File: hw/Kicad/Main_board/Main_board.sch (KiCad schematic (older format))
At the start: 27 parts, among them J1 LIPO 2S, J10 DIST_FRONT, J11 SENSORES_LINEA, J12 DIST_DCHA, J2 MOT_IZQ, J3 TB6612FNG_A, J4 TB6612FNG_B, J5 DC-DC_5V, J6 HC-05, J7 MOT_DER, J8 DIST_IZQ, J9 CAMARA, SW1 SW_DPDT, SW2 SW_Push, SW3 SW_Push, U1 PCF8574

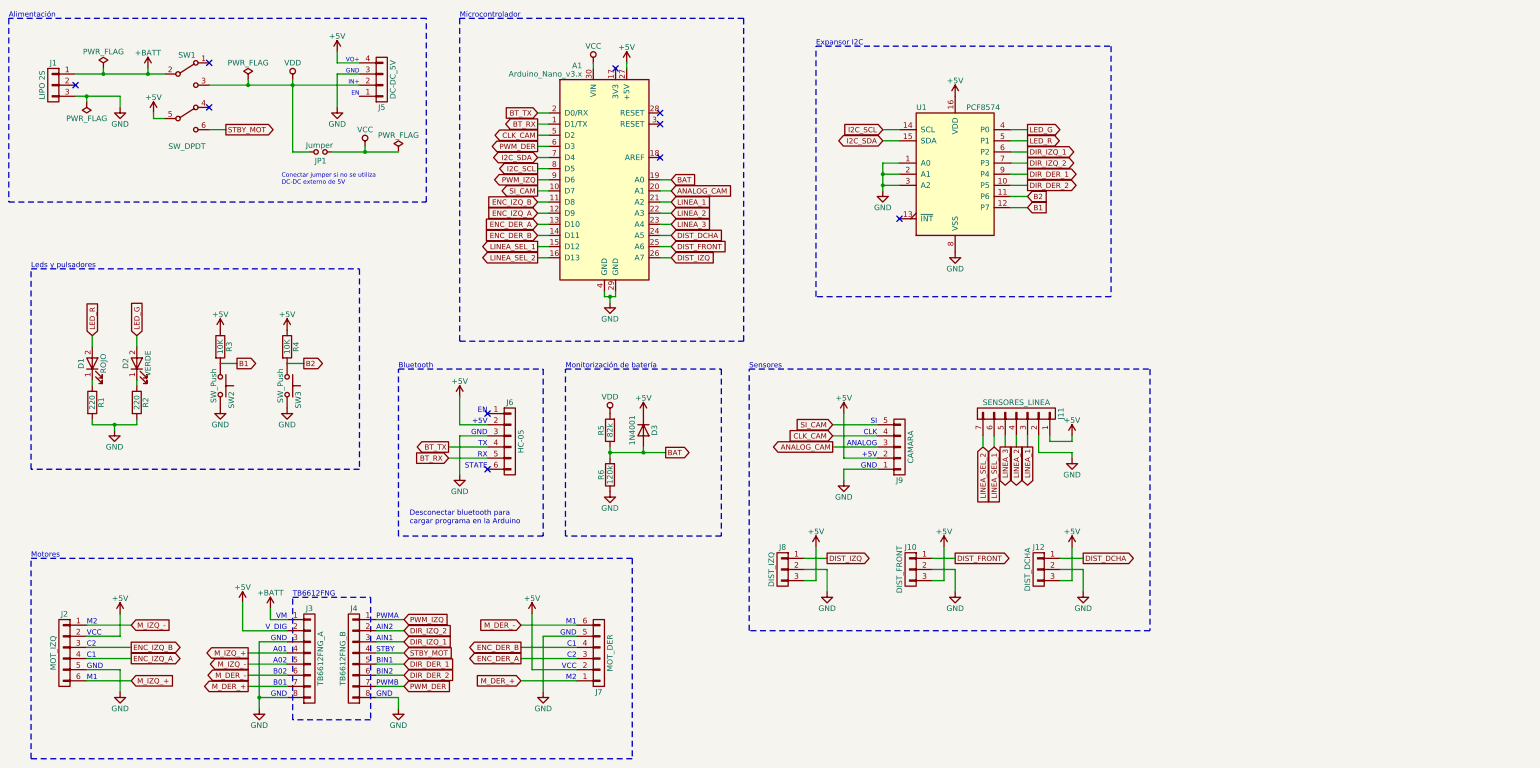
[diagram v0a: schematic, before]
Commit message: Leds connections modified and I2C resistors added
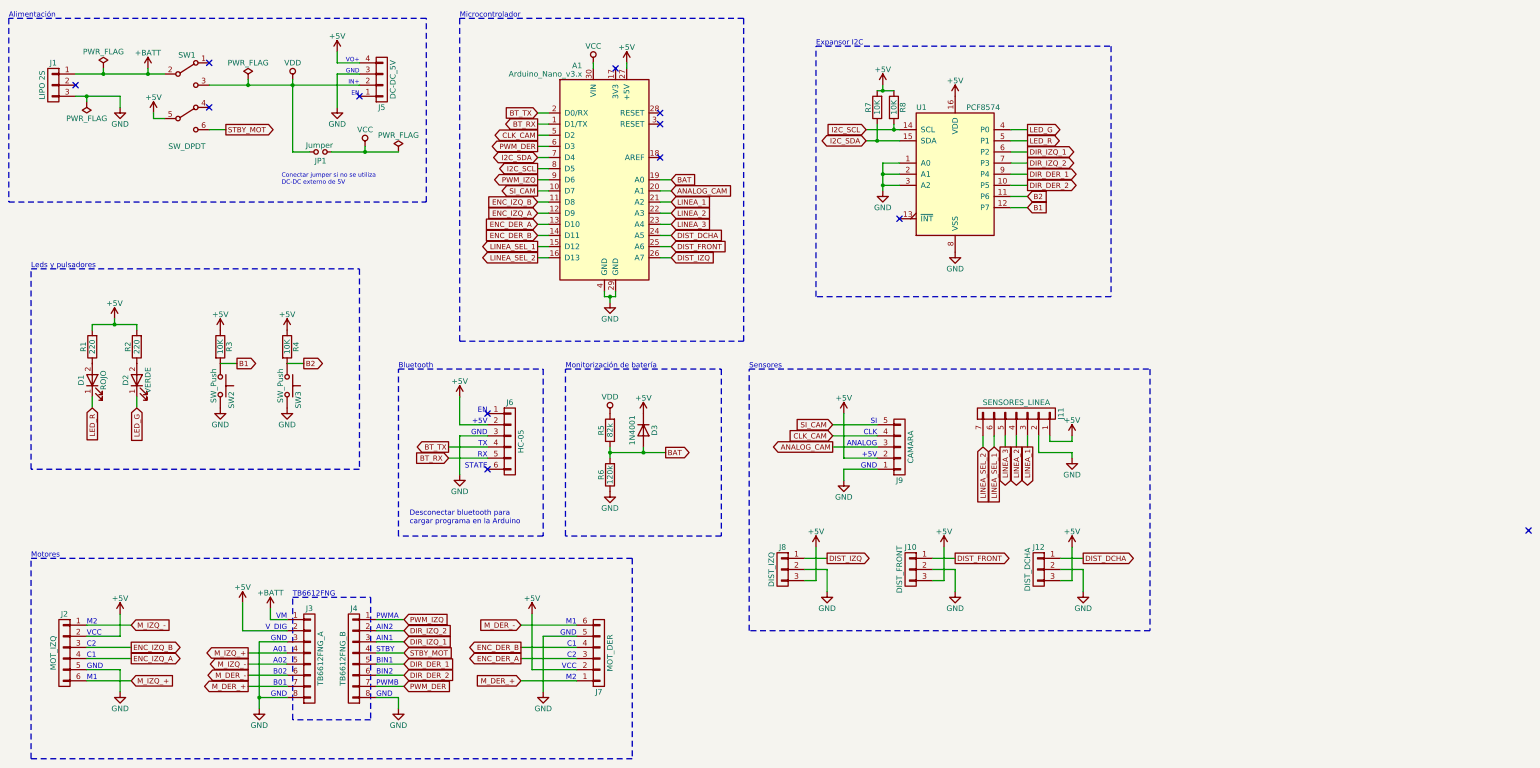
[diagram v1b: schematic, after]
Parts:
- added R7, R8: 10K, Resistors_THT:R_Axial_DIN0207_L6.3mm_D2.5mm_P10.16mm_Horizontal, symbol R
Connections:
- net +5V: now also R1.2, R2.2, R7.2, R8.1
- net GND: no longer R1.2, R2.2
- net I2C_SCL: now also R8.2
- net I2C_SDA: now also R7.1
- net LED_G: now also D2.1 (K); no longer D2.2 (A)
- net LED_R: now also D1.1 (K); no longer D1.2 (A)
- net at R1.1: now also D1.2 (A); no longer D1.1 (K)
- net at R2.1: now also D2.2 (A); no longer D2.1 (K)
- no-connect marks 10 -> 12
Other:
- moved on the sheet: D1, D2, R1, R2

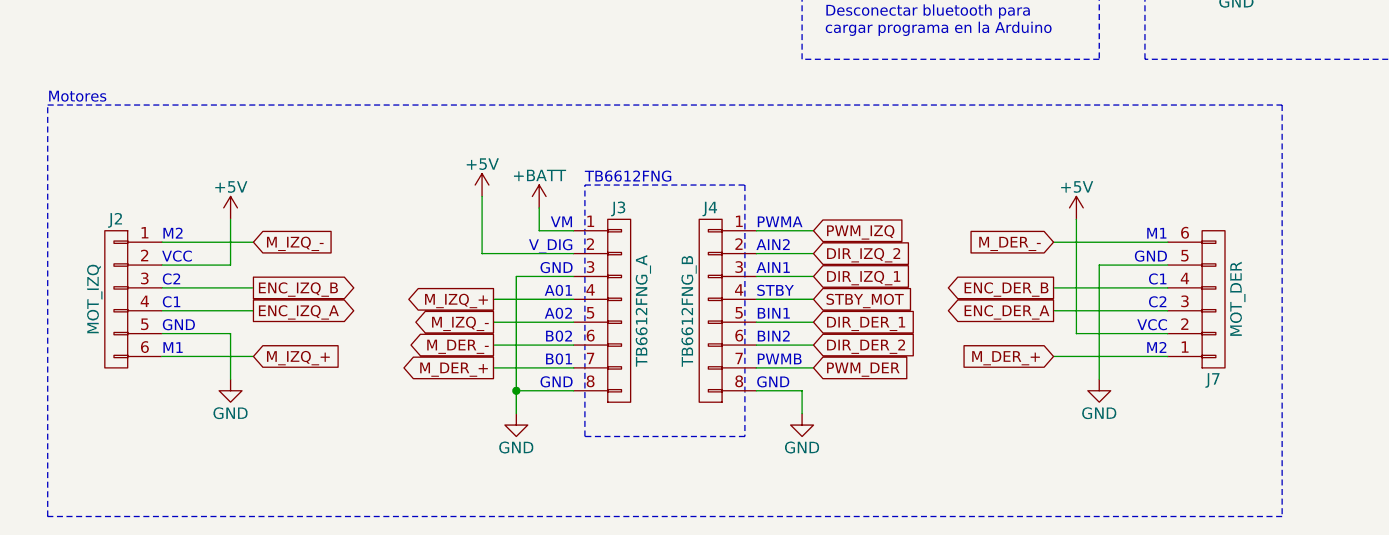
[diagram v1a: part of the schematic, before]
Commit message: Gerbers actualized and motors connector changed
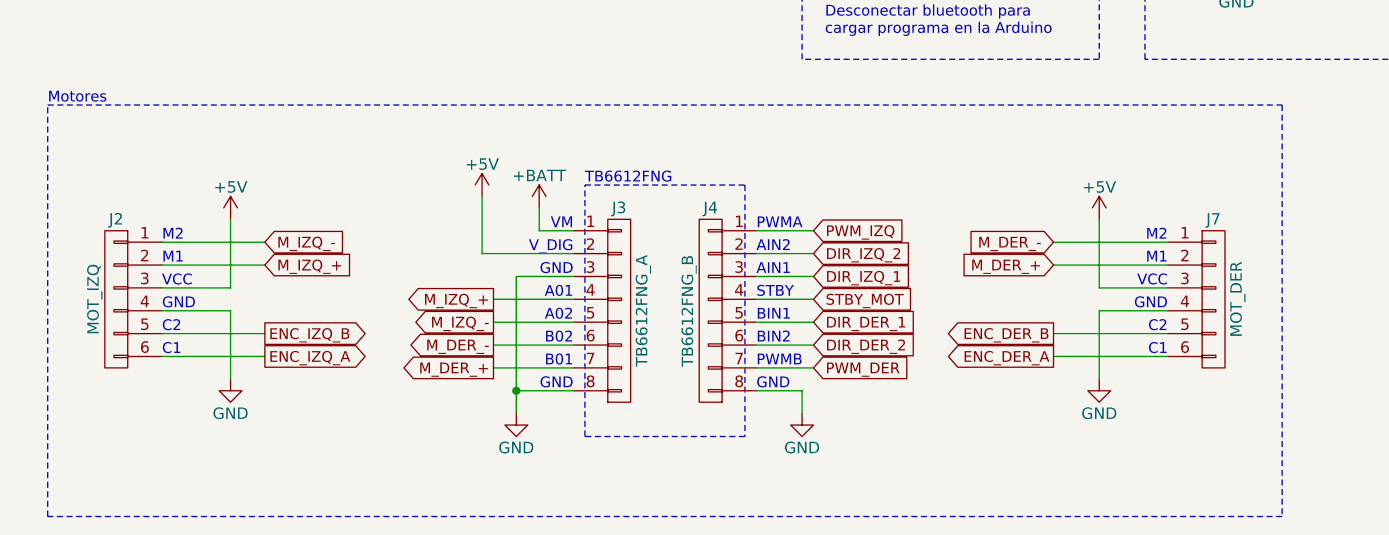
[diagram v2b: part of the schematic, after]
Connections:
- net +5V: now also J2.3 (P3), J7.3 (P3); no longer J2.2 (P2), J7.2 (P2)
- net ENC_DER_A: now also J7.6 (P6); no longer J7.3 (P3)
- net ENC_DER_B: now also J7.5 (P5); no longer J7.4 (P4)
- net ENC_IZQ_A: now also J2.6 (P6); no longer J2.4 (P4)
- net ENC_IZQ_B: now also J2.5 (P5); no longer J2.3 (P3)
- net GND: now also J2.4 (P4), J7.4 (P4); no longer J2.5 (P5), J7.5 (P5)
- net M_DER_+: now also J7.2 (P2); no longer J7.1 (P1)
- net M_DER_-: now also J7.1 (P1); no longer J7.6 (P6)
- net M_IZQ_+: now also J2.2 (P2); no longer J2.6 (P6)
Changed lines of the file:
@@
 F 3 "" H 6050 6500 50  0001 C CNN
 	1    6050 6500
-	1    0    0    1
+	1    0    0    -1
 $EndComp
 $Comp
@@
 L +5V #PWR019
 U 1 1 593E26EB
-P 5450 6150
-F 0 "#PWR019" H 5450 6000 50  0001 C CNN
-F 1 "+5V" H 5450 6290 50  0000 C CNN
-F 2 "" H 5450 6150 50  0001 C CNN
-F 3 "" H 5450 6150 50  0001 C CNN
-	1    5450 6150
+P 5550 6150
+F 0 "#PWR019" H 5550 6000 50  0001 C CNN
+F 1 "+5V" H 5550 6290 50  0000 C CNN
+F 2 "" H 5550 6150 50  0001 C CNN
+F 3 "" H 5550 6150 50  0001 C CNN
+	1    5550 6150
 	1    0    0    -1
 $EndComp
@@
 Text Notes 1450 6250 0    47   ~ 0
 M2
+Text Notes 1450 6350 0    47   ~ 0
+M1
+Text Notes 1450 6450 0    47   ~ 0
+VCC
+Text Notes 1450 6550 0    47   ~ 0
+GND
+Text Notes 1450 6650 0    47   ~ 0
+C2
 Text Notes 1450 6750 0    47   ~ 0
+C1
+Text Notes 5850 6250 2    47   ~ 0
+M2
+Text Notes 5850 6350 2    47   ~ 0
 M1
-Text Notes 1450 6350 0    47   ~ 0
+Text Notes 5850 6550 2    47   ~ 0
+GND
+Text Notes 5850 6450 2    47   ~ 0
 VCC
-Text Notes 1450 6650 0    47   ~ 0
-GND
-Text Notes 1450 6450 0    47   ~ 0
+Text Notes 5850 6650 2    47   ~ 0
 C2
-Text Notes 1450 6550 0    47   ~ 0
+Text Notes 5850 6750 2    47   ~ 0
 C1
-Text Notes 5850 6750 2    47   ~ 0
-M2
-Text Notes 5850 6250 2    47   ~ 0
-M1
-Text Notes 5850 6350 2    47   ~ 0
-GND
-Text Notes 5850 6650 2    47   ~ 0
-VCC
-Text Notes 5850 6550 2    47   ~ 0
-C2
-Text Notes 5850 6450 2    47   ~ 0
-C1
-Text GLabel 1850 6750 2    47   Input ~ 0
+Text GLabel 1900 6350 2    47   Input ~ 0
 M_IZQ_+
-Text GLabel 1850 6250 2    47   Input ~ 0
+Text GLabel 1900 6250 2    47   Input ~ 0
 M_IZQ_-
-Text GLabel 1850 6550 2    47   Output ~ 0
+Text GLabel 1900 6750 2    47   Output ~ 0
 ENC_IZQ_A
-Text GLabel 1850 6450 2    47   Output ~ 0
+Text GLabel 1900 6650 2    47   Output ~ 0
 ENC_IZQ_B
 Text Notes 3300 6000 0    47   ~ 0
@@
 Text GLabel 5350 6250 0    47   Input ~ 0
 M_DER_-
-Text GLabel 5350 6750 0    47   Input ~ 0
+Text GLabel 5350 6350 0    47   Input ~ 0
 M_DER_+
-Text GLabel 5350 6550 0    47   Output ~ 0
+Text GLabel 5350 6750 0    47   Output ~ 0
 ENC_DER_A
-Text GLabel 5350 6450 0    47   Output ~ 0
+Text GLabel 5350 6650 0    47   Output ~ 0
 ENC_DER_B
 Text Notes 950  5650 0    47   ~ 0
@@
 	4050 6900 4250 6900
 Wire Wire Line
-	1450 6250 1850 6250
-Wire Wire Line
-	1450 6350 1750 6350
-Wire Wire Line
-	1850 6450 1450 6450
-Wire Wire Line
-	1850 6550 1450 6550
-Wire Wire Line
-	1450 6650 1750 6650
-Wire Wire Line
-	1850 6750 1450 6750
+	1450 6250 1900 6250
 Wire Wire Line
 	3100 6200 3100 6100
@@
 	5350 6250 5850 6250
 Wire Wire Line
-	5550 6350 5850 6350
-Wire Wire Line
-	5350 6450 5850 6450
-Wire Wire Line
-	5350 6550 5850 6550
-Wire Wire Line
-	5450 6650 5850 6650
-Wire Wire Line
 	5350 6750 5850 6750
 Wire Wire Line
-	1750 6350 1750 6150
-Wire Wire Line
-	1750 6650 1750 6850
+	1750 6550 1750 6850
 Wire Notes Line
 	3300 6000 4000 6000
@@
 Wire Notes Line
 	3300 7100 3300 6000
-Wire Wire Line
-	5450 6150 5450 6650
-Wire Wire Line
-	5550 6350 5550 6850
 Wire Notes Line
 	950  5650 6350 5650
@@
 NoConn ~ 3900 1500
 NoConn ~ 14400 5400
+Wire Wire Line
+	1450 6350 1900 6350
+Wire Wire Line
+	1750 6150 1750 6450
+Wire Wire Line
+	1750 6450 1450 6450
+Wire Wire Line
+	1450 6550 1750 6550
+Wire Wire Line
+	1450 6650 1900 6650
+Wire Wire Line
+	1900 6750 1450 6750
+Wire Wire Line
+	5350 6350 5850 6350
+Wire Wire Line
+	5550 6150 5550 6450
+Wire Wire Line
+	5550 6450 5850 6450
+Wire Wire Line
+	5550 6850 5550 6550
+Wire Wire Line
+	5550 6550 5850 6550
+Wire Wire Line
+	5350 6650 5850 6650
 $EndSCHEMATC

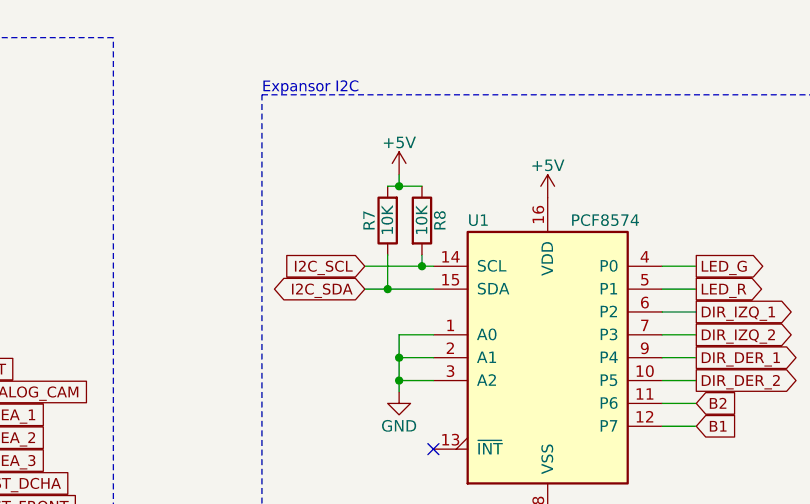
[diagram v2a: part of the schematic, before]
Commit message: I2C resistor values changed
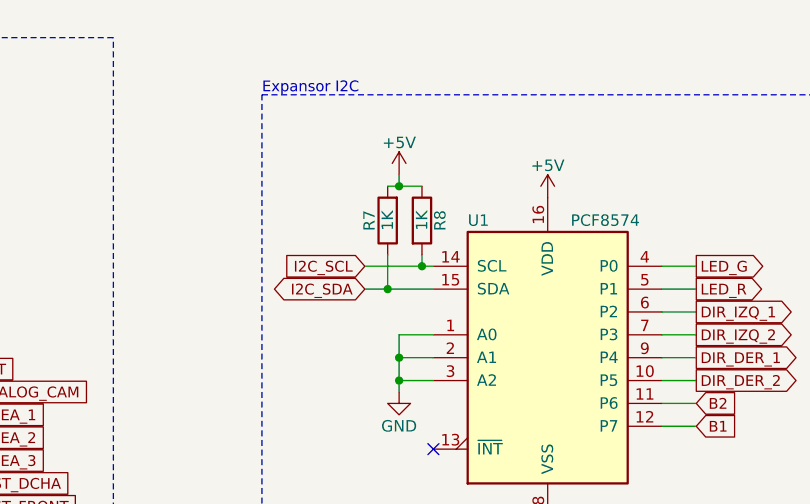
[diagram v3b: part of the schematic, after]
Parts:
- R7, R8: value 10K -> 1K
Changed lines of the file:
@@
 P 8550 1600
 F 0 "R7" V 8630 1600 50  0000 C CNN
-F 1 "10K" V 8550 1600 50  0000 C CNN
+F 1 "1K" V 8550 1600 50  0000 C CNN
 F 2 "Resistors_THT:R_Axial_DIN0207_L6.3mm_D2.5mm_P10.16mm_Horizontal" V 8480 1600 50  0001 C CNN
 F 3 "" H 8550 1600 50  0001 C CNN
@@
 P 8700 1600
 F 0 "R8" V 8780 1600 50  0000 C CNN
-F 1 "10K" V 8700 1600 50  0000 C CNN
+F 1 "1K" V 8700 1600 50  0000 C CNN
 F 2 "Resistors_THT:R_Axial_DIN0207_L6.3mm_D2.5mm_P10.16mm_Horizontal" V 8630 1600 50  0001 C CNN
 F 3 "" H 8700 1600 50  0001 C CNN
